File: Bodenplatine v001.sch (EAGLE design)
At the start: 113 parts, among them K1 RY612012, K2 RY612012, K3 RY612012, K4 RY612012, K5 RY612012, K6 RY612012, K7 RY612012, K8 RY612012, K9 RY612012, Q1 BC846BLT1SMD, Q2 BC846BLT1SMD, Q3 BC846BLT1SMD, Q4 BC846BLT1SMD, Q5 BC846BLT1SMD, Q6 BC846BLT1SMD, Q7 BC846BLT1SMD, Q8 BC846BLT1SMD, Q9 BC846BLT1SMD, X1 SPRINGCON_AST125_5X2, X10 SPRINGCON_AST125_3X2, X11 SPRINGCON_AST125_4X2, X12 SPRINGCON_AST125_4X2, X13 SPRINGCON_AST125_5X2, X14 236-403, X15 236-402, X2 SPRINGCON_AST125_5X2, X3 SPRINGCON_AST125_5X2, X4 SPRINGCON_AST125_5X2, X5 SPRINGCON_AST125_5X2, X6 SPRINGCON_AST125_5X2, X7 SPRINGCON_AST125_5X2, X8 SPRINGCON_AST125_5X2, X9 SPRINGCON_AST125_5X2

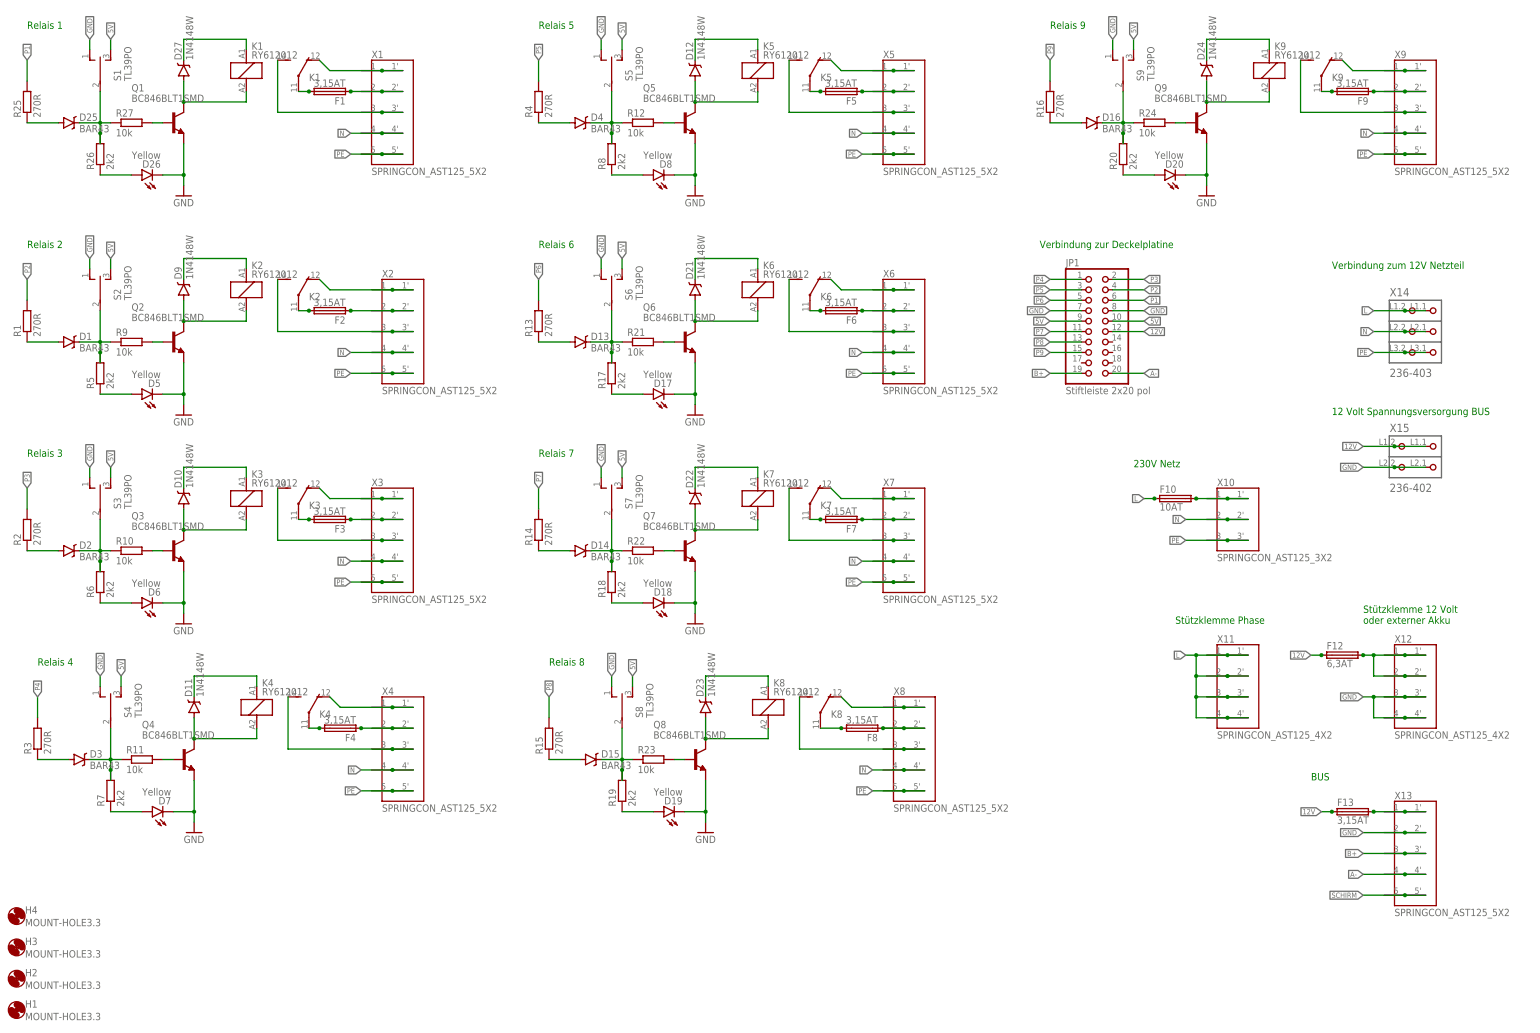
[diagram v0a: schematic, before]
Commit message: Vertauschte Dioden gefixt
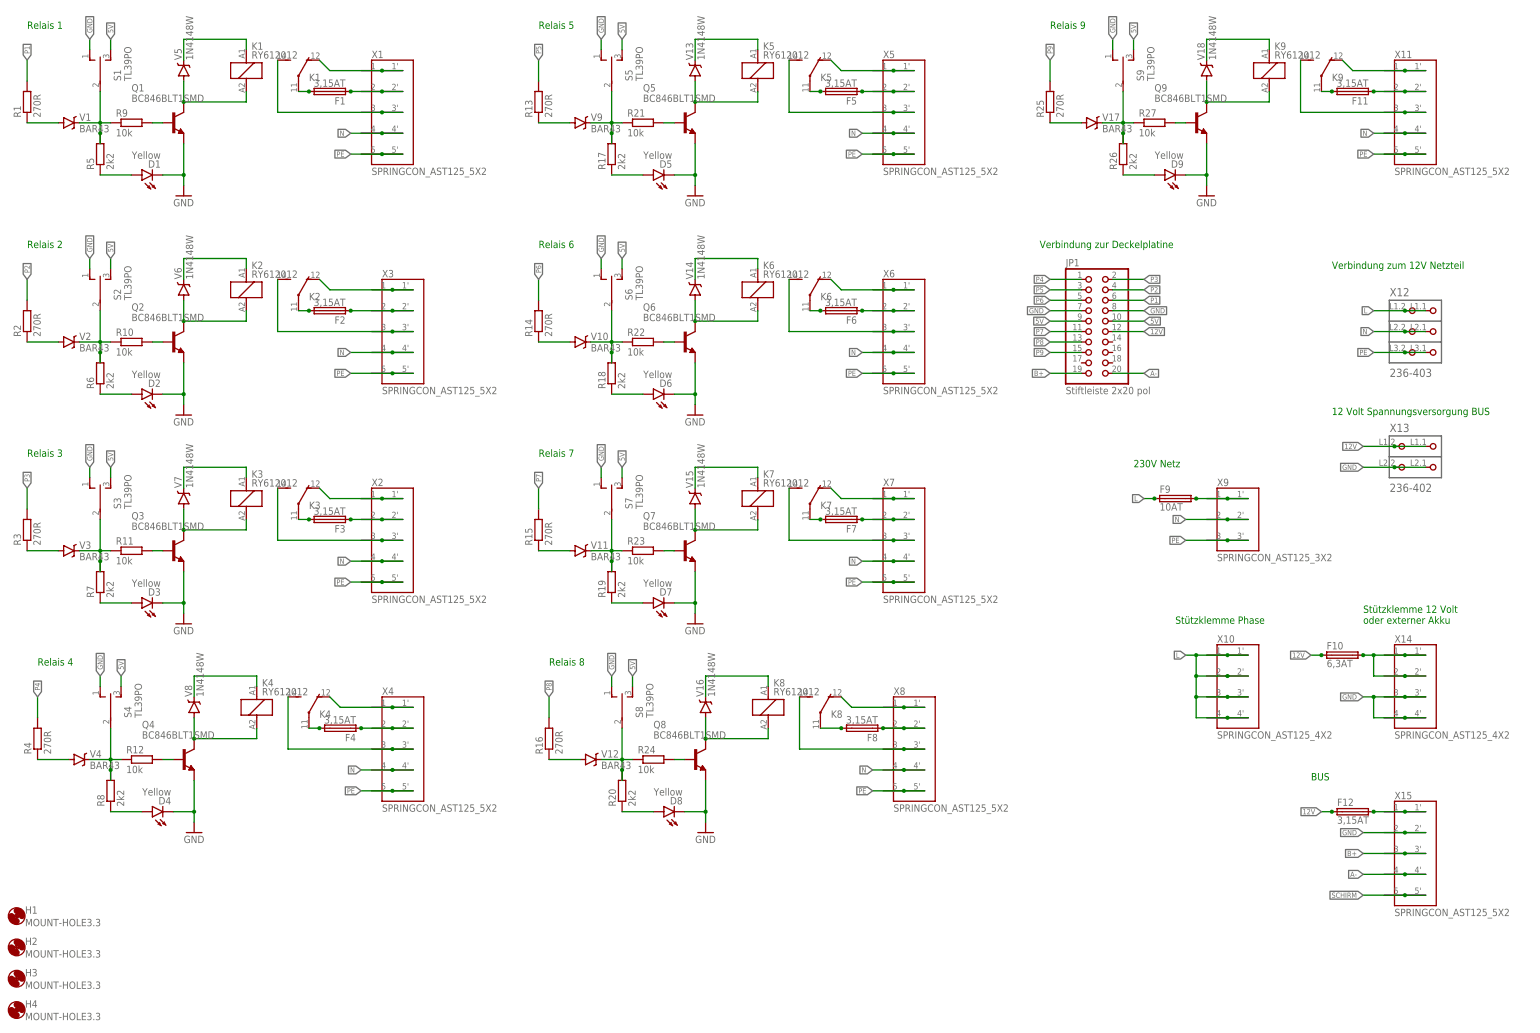
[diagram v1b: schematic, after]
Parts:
- removed D17, D18, D19, D20, D26: Yellow, SparkFun-LED:LED-YELLOW0603
- removed F13: 3,15AT, xMZ-Mod-Touch-Bodenplatine:FPG4
- added F11: 3,15AT, xMZ-Mod-Touch-Bodenplatine:FPG4
- added V2, V3, V4, V9: BAR43, xMZ-Mod-Touch-Bodenplatine:BAR43
- added V6: 1N4148W, xMZ-Mod-Touch-Bodenplatine:LL4148
- D1, D2, D3, D4: value BAR43 -> Yellow; device xMZ-Mod-Touch-Bodenplatine:BAR43 -> SparkFun-LED:LED-YELLOW0603; MF FAIRCHILD SEMICONDUCTOR -> KINGBRIGHT; MPN BAR43 -> KP-3216SYC; OC_FARNELL (none) -> 8529990
- D9: value 1N4148W -> Yellow; device xMZ-Mod-Touch-Bodenplatine:LL4148 -> SparkFun-LED:LED-YELLOW0603; MF VISHAY -> KINGBRIGHT; MPN LL4148-GS08 -> KP-3216SYC; OC_FARNELL (none) -> 8529990
- F10: value 10AT -> 6,3AT
- F12: value 6,3AT -> 3,15AT
- F9: value 3,15AT -> 10AT
- X10: value SPRINGCON_AST125_3X2 -> SPRINGCON_AST125_4X2; device xMZ-Mod-Touch-Bodenplatine:SPRINGCON_AST125_3X2 -> xMZ-Mod-Touch-Bodenplatine:SPRINGCON_AST125_4X2
- X11: value SPRINGCON_AST125_4X2 -> SPRINGCON_AST125_5X2; device xMZ-Mod-Touch-Bodenplatine:SPRINGCON_AST125_4X2 -> xMZ-Mod-Touch-Bodenplatine:SPRINGCON_AST125_5X2
- X12: value SPRINGCON_AST125_4X2 -> 236-403; device xMZ-Mod-Touch-Bodenplatine:SPRINGCON_AST125_4X2 -> con-wago_236:236-403; MF (none) -> WAGO; MPN (none) -> 236-403; OC_FARNELL unknown -> 1283527
- X13: value SPRINGCON_AST125_5X2 -> 236-402; device xMZ-Mod-Touch-Bodenplatine:SPRINGCON_AST125_5X2 -> con-wago_236:236-402; MF (none) -> WAGO; MPN (none) -> 236-402; OC_FARNELL unknown -> 1283526
- X14: value 236-403 -> SPRINGCON_AST125_4X2; device con-wago_236:236-403 -> xMZ-Mod-Touch-Bodenplatine:SPRINGCON_AST125_4X2; MF WAGO -> (none); MPN 236-403 -> (none); OC_FARNELL 1283527 -> unknown
- X15: value 236-402 -> SPRINGCON_AST125_5X2; device con-wago_236:236-402 -> xMZ-Mod-Touch-Bodenplatine:SPRINGCON_AST125_5X2; MF WAGO -> (none); MPN 236-402 -> (none); OC_FARNELL 1283526 -> unknown
- X9: value SPRINGCON_AST125_5X2 -> SPRINGCON_AST125_3X2; device xMZ-Mod-Touch-Bodenplatine:SPRINGCON_AST125_5X2 -> xMZ-Mod-Touch-Bodenplatine:SPRINGCON_AST125_3X2
- renumbered D10 to V7, D11 to V8, D12 to V13, D13 to V10, D14 to V11, D15 to V12, D16 to V17, D21 to V14, D22 to V15, D23 to V16, D24 to V18, D25 to V1, D27 to V5
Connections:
- net 12V: now also F10.1, F10.1@2, X13.P1.1, X13.P1.2; no longer F13.1, F13.1@2, X15.P1.1, X15.P1.2
- net A-: now also X15.4@1, X15.4@2; no longer X13.4@1, X13.4@2
- net B+: now also X15.3@1, X15.3@2; no longer X13.3@1, X13.3@2
- net GND: now also D1.C, D2.C, D3.C, D4.C, D9.C, X13.P2.1, X13.P2.2, X14.3@1, X14.3@2, X14.4@1, X14.4@2, X15.2@1, X15.2@2; no longer D17.C, D18.C, D19.C, D20.C, D26.C, X12.3@1, X12.3@2, X12.4@1, X12.4@2, X13.2@1, X13.2@2, X15.P2.1, X15.P2.2
- net L: now also F9.1, F9.1@2, X10.1@1, X10.1@2, X10.2@1, X10.2@2, X10.3@1, X10.3@2, X10.4@1, X10.4@2, X12.P1.1, X12.P1.2; no longer F10.1, F10.1@2, X11.1@1, X11.1@2, X11.2@1, X11.2@2, X11.3@1, X11.3@2, X11.4@1, X11.4@2, X14.P1.1, X14.P1.2
- net N: now also X11.4@1, X11.4@2, X12.P2.1, X12.P2.2, X9.2@1, X9.2@2; no longer X10.2@1, X10.2@2, X14.P2.1, X14.P2.2, X9.4@1, X9.4@2
- net N$1: now also X3.2@1, X3.2@2; no longer X2.2@1, X2.2@2
- net N$10: now also R10.2; no longer R9.2
- net N$11: now also V6.C; no longer D9.C
- net N$13: now also R3.1, V3.A; no longer D2.A, R2.1
- net N$14: now also R11.1, R7.2, V3.C; no longer D2.C, R10.1, R6.2
- net N$15: now also D3.A, R7.1; no longer D6.A, R6.1
- net N$16: now also R11.2; no longer R10.2
- net N$19: now also X2.2@1, X2.2@2; no longer X3.2@1, X3.2@2
- net N$2: now also X3.3@1, X3.3@2; no longer X2.3@1, X2.3@2
- net N$20: now also X2.1@1, X2.1@2; no longer X3.1@1, X3.1@2
- net N$23: now also R4.1, V4.A; no longer D3.A, R3.1
- net N$24: now also R12.1, R8.2, V4.C; no longer D3.C, R11.1, R7.2
- net N$25: now also D4.A, R8.1; no longer D7.A, R7.1
- net N$26: now also R12.2; no longer R11.2
- net N$33: now also R13.1, V9.A; no longer D4.A, R4.1
- net N$34: now also R17.2, R21.1, V9.C; no longer D4.C, R12.1, R8.2
- net N$35: now also D5.A, R17.1; no longer D8.A, R8.1
- net N$36: now also R21.2; no longer R12.2
- net N$4: now also X3.1@1, X3.1@2; no longer X2.1@1, X2.1@2
- net N$43: now also R14.1; no longer R13.1
- net N$44: now also R18.2, R22.1; no longer R17.2, R21.1
- net N$45: now also D6.A, R18.1; no longer D17.A, R17.1
- net N$46: now also R22.2; no longer R21.2
- net N$5: now also V6.A; no longer D9.A
- net N$53: now also R15.1; no longer R14.1
- net N$54: now also R19.2, R23.1; no longer R18.2, R22.1
- net N$55: now also D7.A, R19.1; no longer D18.A, R18.1
- net N$56: now also R23.2; no longer R22.2
- net N$6: now also X2.3@1, X2.3@2; no longer X3.3@1, X3.3@2
- net N$63: now also R16.1; no longer R15.1
- net N$64: now also R20.2, R24.1; no longer R19.2, R23.1
- net N$65: now also D8.A, R20.1; no longer D19.A, R19.1
- net N$66: now also R24.2; no longer R23.2
- net N$7: now also R2.1, V2.A; no longer D1.A, R1.1
- net N$71: now also X11.3@1, X11.3@2; no longer X9.3@1, X9.3@2
- net N$72: now also F11.2, F11.2@2; no longer F9.2, F9.2@2
- net N$73: now also R25.1; no longer R16.1
- net N$74: now also R26.2, R27.1; no longer R20.2, R24.1
- net N$75: now also D9.A, R26.1; no longer D20.A, R20.1
- net N$76: now also R27.2; no longer R24.2
- net N$79: now also F11.1, F11.1@2, X11.2@1, X11.2@2; no longer F9.1, F9.1@2, X9.2@1, X9.2@2
- net N$8: now also R10.1, R6.2, V2.C; no longer D1.C, R5.2, R9.1
- net N$80: now also X11.1@1, X11.1@2; no longer X9.1@1, X9.1@2
- net N$83: now also R1.1; no longer R25.1
- net N$84: now also R5.2, R9.1; no longer R26.2, R27.1
- net N$85: now also D1.A, R5.1; no longer D26.A, R26.1
- net N$86: now also R9.2; no longer R27.2
- net N$9: now also D2.A, R6.1; no longer D5.A, R5.1
- net N$91: now also F9.2, F9.2@2, X9.1@1, X9.1@2; no longer F10.2, F10.2@2, X10.1@1, X10.1@2
- net N$92: now also F12.2, F12.2@2, X15.1@1, X15.1@2; no longer F13.2, F13.2@2, X13.1@1, X13.1@2
- net N$94: now also F10.2, F10.2@2, X14.1@1, X14.1@2, X14.2@1, X14.2@2; no longer F12.2, F12.2@2, X12.1@1, X12.1@2, X12.2@1, X12.2@2
- net P1: now also R1.2; no longer R25.2
- net P2: now also R2.2; no longer R1.2
- net P3: now also R3.2; no longer R2.2
- net P4: now also R4.2; no longer R3.2
- net P5: now also R13.2; no longer R4.2
- net P6: now also R14.2; no longer R13.2
- net P7: now also R15.2; no longer R14.2
- net P8: now also R16.2; no longer R15.2
- net P9: now also R25.2; no longer R16.2
- net PE: now also X11.5@1, X11.5@2, X12.P3.1, X12.P3.2, X9.3@1, X9.3@2; no longer X10.3@1, X10.3@2, X14.P3.1, X14.P3.2, X9.5@1, X9.5@2
- net SCHIRM: now also X15.5@1, X15.5@2; no longer X13.5@1, X13.5@2
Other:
- moved on the sheet: D5, D6, D7, D8, F10, F12, F9, H1, H2, H3, H4, R1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

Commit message: Begin Änderungen der Klemmenbezeichnungen
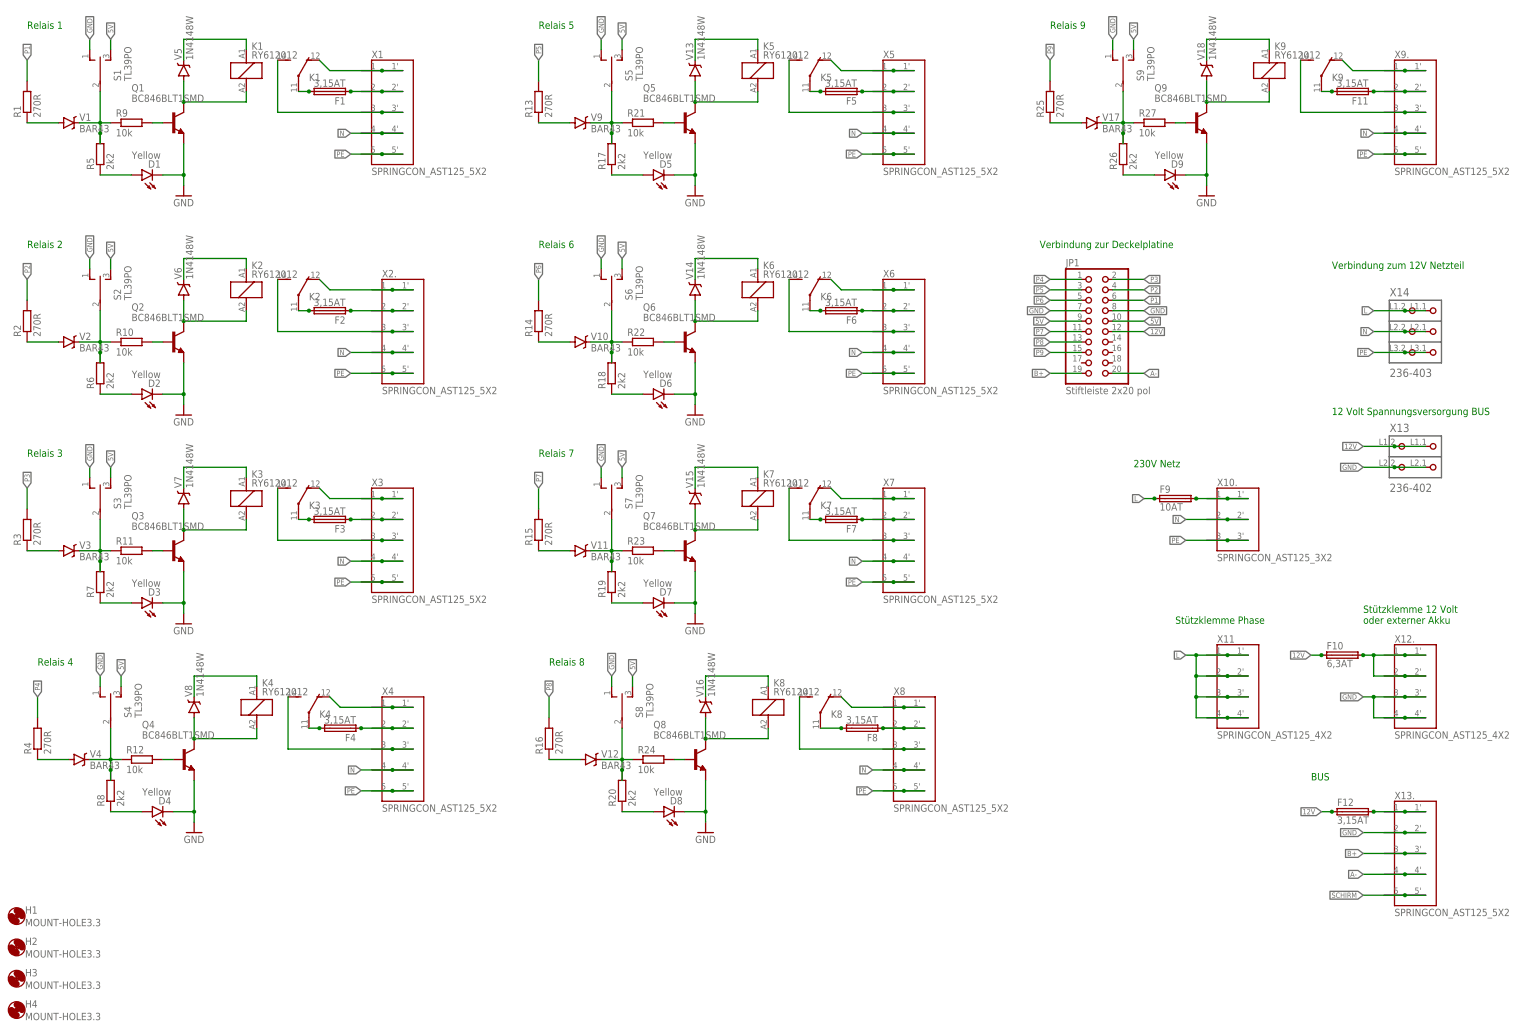
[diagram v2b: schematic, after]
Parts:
- removed X10: SPRINGCON_AST125_4X2, xMZ-Mod-Touch-Bodenplatine:SPRINGCON_AST125_4X2
- removed X12: 236-403, con-wago_236:236-403
- removed X2: SPRINGCON_AST125_5X2, xMZ-Mod-Touch-Bodenplatine:SPRINGCON_AST125_5X2
- added X12.: SPRINGCON_AST125_4X2, xMZ-Mod-Touch-Bodenplatine:SPRINGCON_AST125_4X2
- added X2., X9.: SPRINGCON_AST125_5X2, xMZ-Mod-Touch-Bodenplatine:SPRINGCON_AST125_5X2
- X11: value SPRINGCON_AST125_5X2 -> SPRINGCON_AST125_4X2; device xMZ-Mod-Touch-Bodenplatine:SPRINGCON_AST125_5X2 -> xMZ-Mod-Touch-Bodenplatine:SPRINGCON_AST125_4X2
- X14: value SPRINGCON_AST125_4X2 -> 236-403; device xMZ-Mod-Touch-Bodenplatine:SPRINGCON_AST125_4X2 -> con-wago_236:236-403; MF (none) -> WAGO; MPN (none) -> 236-403; OC_FARNELL unknown -> 1283527
- renumbered X15 to X13., X9 to X10.
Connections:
- net GND: now also X12..3@1, X12..3@2, X12..4@1, X12..4@2; no longer X14.3@1, X14.3@2, X14.4@1, X14.4@2
- net L: now also X11.1@1, X11.1@2, X11.2@1, X11.2@2, X11.3@1, X11.3@2, X11.4@1, X11.4@2, X14.P1.1, X14.P1.2; no longer X10.1@1, X10.1@2, X10.2@1, X10.2@2, X10.3@1, X10.3@2, X10.4@1, X10.4@2, X12.P1.1, X12.P1.2
- net N: now also X14.P2.1, X14.P2.2, X2..4@1, X2..4@2, X9..4@1, X9..4@2; no longer X11.4@1, X11.4@2, X12.P2.1, X12.P2.2, X2.4@1, X2.4@2
- net N$1: now also X2..2@1, X2..2@2; no longer X3.2@1, X3.2@2
- net N$19: now also X3.2@1, X3.2@2; no longer X2.2@1, X2.2@2
- net N$2: now also X2..3@1, X2..3@2; no longer X3.3@1, X3.3@2
- net N$20: now also X3.1@1, X3.1@2; no longer X2.1@1, X2.1@2
- net N$4: now also X2..1@1, X2..1@2; no longer X3.1@1, X3.1@2
- net N$6: now also X3.3@1, X3.3@2; no longer X2.3@1, X2.3@2
- net N$71: now also X9..3@1, X9..3@2; no longer X11.3@1, X11.3@2
- net N$79: now also X9..2@1, X9..2@2; no longer X11.2@1, X11.2@2
- net N$80: now also X9..1@1, X9..1@2; no longer X11.1@1, X11.1@2
- net N$94: now also X12..1@1, X12..1@2, X12..2@1, X12..2@2; no longer X14.1@1, X14.1@2, X14.2@1, X14.2@2
- net PE: now also X14.P3.1, X14.P3.2, X2..5@1, X2..5@2, X9..5@1, X9..5@2; no longer X11.5@1, X11.5@2, X12.P3.1, X12.P3.2, X2.5@1, X2.5@2
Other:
- moved on the sheet: X3

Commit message: Erste finale Version OHNE CHECKS
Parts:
- removed F11: 3,15AT, xMZ-Mod-Touch-Bodenplatine:FPG4
- removed X13.: SPRINGCON_AST125_5X2, xMZ-Mod-Touch-Bodenplatine:SPRINGCON_AST125_5X2
- added F13: 3,15AT, xMZ-Mod-Touch-Bodenplatine:FPG4
- added X15: 236-402, xMZ-Mod-Touch-Bodenplatine:236-402
- F10: value 6,3AT -> 10AT
- F12: value 3,15AT -> 6,3AT
- F9: value 10AT -> 3,15AT
- X13: value 236-402 -> SPRINGCON_AST125_5X2; device con-wago_236:236-402 -> xMZ-Mod-Touch-Bodenplatine:SPRINGCON_AST125_5X2; MF WAGO -> (none); MPN 236-402 -> (none); OC_FARNELL 1283526 -> unknown
- X14: device con-wago_236:236-403 -> xMZ-Mod-Touch-Bodenplatine:236-403
- renumbered X10. to X10, X12. to X12, X2. to X2, X9. to X9
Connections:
- net 12V: now also F13.1, F13.1@2, X15.P1.1, X15.P1.2; no longer F10.1, F10.1@2, X13.P1.1, X13.P1.2
- net A-: now also X13.4@1, X13.4@2; no longer X13..4@1, X13..4@2
- net B+: now also X13.3@1, X13.3@2; no longer X13..3@1, X13..3@2
- net GND: now also X13.2@1, X13.2@2, X15.P2.1, X15.P2.2; no longer X13..2@1, X13..2@2, X13.P2.1, X13.P2.2
- net L: now also F10.1, F10.1@2; no longer F9.1, F9.1@2
- net N$72: now also F9.2, F9.2@2; no longer F11.2, F11.2@2
- net N$79: now also F9.1, F9.1@2; no longer F11.1, F11.1@2
- net N$91: now also F10.2, F10.2@2; no longer F9.2, F9.2@2
- net N$92: now also F13.2, F13.2@2, X13.1@1, X13.1@2; no longer F12.2, F12.2@2, X13..1@1, X13..1@2
- net N$94: now also F12.2, F12.2@2; no longer F10.2, F10.2@2
- net SCHIRM: now also X13.5@1, X13.5@2; no longer X13..5@1, X13..5@2
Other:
- moved on the sheet: F10, F12, F9
